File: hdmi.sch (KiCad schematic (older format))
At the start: 0 parts

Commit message: HDMI and VGA circuit added.
Signed-off-by: Kali Prasad <kprasadvnsi@protonmail.com>
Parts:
- added J?: HDMI_A, symbol Connector:HDMI_A
- added R? (x8): 270, symbol Device:R
- added R?: 1K, symbol Device:R
- added R?: R, symbol Device:R
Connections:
- net labels added: +5V, GND
- wire segments 0 -> 33
- no-connect marks 0 -> 4
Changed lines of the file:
@@
 Comment4 ""
 $EndDescr
+$Comp
+L Connector:HDMI_A J?
+U 1 1 5D63985F
+P 8050 3500
+F 0 "J?" H 8480 3546 50  0000 L CNN
+F 1 "HDMI_A" H 8480 3455 50  0000 L CNN
+F 2 "" H 8075 3500 50  0001 C CNN
+F 3 "https://en.wikipedia.org/wiki/HDMI" H 8075 3500 50  0001 C CNN
+	1    8050 3500
+	1    0    0    -1
+$EndComp
+$Comp
+L Device:R R?
+U 1 1 5D63B505
+P 7200 2700
+F 0 "R?" V 7150 2450 50  0000 C CNN
+F 1 "270" V 7150 2900 50  0000 C CNN
+F 2 "" V 7130 2700 50  0001 C CNN
+F 3 "~" H 7200 2700 50  0001 C CNN
+	1    7200 2700
+	0    1    1    0
+$EndComp
+Wire Wire Line
+	7350 2700 7650 2700
+Wire Wire Line
+	7050 2700 6750 2700
+$Comp
+L Device:R R?
+U 1 1 5D63DE7F
+P 7200 2800
+F 0 "R?" V 7150 2550 50  0000 C CNN
+F 1 "270" V 7150 3000 50  0000 C CNN
+F 2 "" V 7130 2800 50  0001 C CNN
+F 3 "~" H 7200 2800 50  0001 C CNN
+	1    7200 2800
+	0    1    1    0
+$EndComp
+Wire Wire Line
+	7350 2800 7650 2800
+Wire Wire Line
+	7050 2800 6750 2800
+$Comp
+L Device:R R?
+U 1 1 5D63FCB8
+P 7200 2900
+F 0 "R?" V 7150 2650 50  0000 C CNN
+F 1 "270" V 7150 3100 50  0000 C CNN
+F 2 "" V 7130 2900 50  0001 C CNN
+F 3 "~" H 7200 2900 50  0001 C CNN
+	1    7200 2900
+	0    1    1    0
+$EndComp
+Wire Wire Line
+	7350 2900 7650 2900
+Wire Wire Line
+	7050 2900 6750 2900
+$Comp
+L Device:R R?
+U 1 1 5D63FCC4
+P 7200 3000
+F 0 "R?" V 7150 2750 50  0000 C CNN
+F 1 "270" V 7150 3200 50  0000 C CNN
+F 2 "" V 7130 3000 50  0001 C CNN
+F 3 "~" H 7200 3000 50  0001 C CNN
+	1    7200 3000
+	0    1    1    0
+$EndComp
+Wire Wire Line
+	7350 3000 7650 3000
+Wire Wire Line
+	7050 3000 6750 3000
+$Comp
+L Device:R R?
+U 1 1 5D6413F6
+P 7200 3100
+F 0 "R?" V 7150 2850 50  0000 C CNN
+F 1 "270" V 7150 3300 50  0000 C CNN
+F 2 "" V 7130 3100 50  0001 C CNN
+F 3 "~" H 7200 3100 50  0001 C CNN
+	1    7200 3100
+	0    1    1    0
+$EndComp
+Wire Wire Line
+	7350 3100 7650 3100
+Wire Wire Line
+	7050 3100 6750 3100
+$Comp
+L Device:R R?
+U 1 1 5D641402
+P 7200 3200
+F 0 "R?" V 7150 2950 50  0000 C CNN
+F 1 "270" V 7150 3400 50  0000 C CNN
+F 2 "" V 7130 3200 50  0001 C CNN
+F 3 "~" H 7200 3200 50  0001 C CNN
+	1    7200 3200
+	0    1    1    0
+$EndComp
+Wire Wire Line
+	7350 3200 7650 3200
+Wire Wire Line
+	7050 3200 6750 3200
+$Comp
+L Device:R R?
+U 1 1 5D64140E
+P 7200 3300
+F 0 "R?" V 7150 3050 50  0000 C CNN
+F 1 "270" V 7150 3500 50  0000 C CNN
+F 2 "" V 7130 3300 50  0001 C CNN
+F 3 "~" H 7200 3300 50  0001 C CNN
+	1    7200 3300
+	0    1    1    0
+$EndComp
+Wire Wire Line
+	7350 3300 7650 3300
+Wire Wire Line
+	7050 3300 6750 3300
+$Comp
+L Device:R R?
+U 1 1 5D64141A
+P 7200 3400
+F 0 "R?" V 7150 3150 50  0000 C CNN
+F 1 "270" V 7150 3600 50  0000 C CNN
+F 2 "" V 7130 3400 50  0001 C CNN
+F 3 "~" H 7200 3400 50  0001 C CNN
+	1    7200 3400
+	0    1    1    0
+$EndComp
+Wire Wire Line
+	7350 3400 7650 3400
+Wire Wire Line
+	7050 3400 6750 3400
+NoConn ~ 7650 3600
+NoConn ~ 7650 3800
+NoConn ~ 7650 3900
+NoConn ~ 7650 4100
+$Comp
+L Device:R R?
+U 1 1 5D64A665
+P 7550 4450
+F 0 "R?" H 7400 4600 50  0000 L CNN
+F 1 "1K" H 7400 4350 50  0000 L CNN
+F 2 "" V 7480 4450 50  0001 C CNN
+F 3 "~" H 7550 4450 50  0001 C CNN
+	1    7550 4450
+	1    0    0    -1
+$EndComp
+Wire Wire Line
+	7650 4200 7550 4200
+Wire Wire Line
+	7550 4200 7550 4300
+$Comp
+L power:GND #PWR?
+U 1 1 5D64BC4F
+P 7550 4700
+F 0 "#PWR?" H 7550 4450 50  0001 C CNN
+F 1 "GND" H 7555 4527 50  0000 C CNN
+F 2 "" H 7550 4700 50  0001 C CNN
+F 3 "" H 7550 4700 50  0001 C CNN
+	1    7550 4700
+	1    0    0    -1
+$EndComp
+Wire Wire Line
+	7550 4600 7550 4700
+Wire Wire Line
+	7850 4600 7850 4700
+Wire Wire Line
+	7850 4700 7950 4700
+Wire Wire Line
+	8350 4700 8350 4600
+Wire Wire Line
+	8250 4600 8250 4700
+Connection ~ 8250 4700
+Wire Wire Line
+	8250 4700 8350 4700
+Wire Wire Line
+	8150 4600 8150 4700
+Connection ~ 8150 4700
+Wire Wire Line
+	8150 4700 8250 4700
+Wire Wire Line
+	8050 4600 8050 4700
+Connection ~ 8050 4700
+Wire Wire Line
+	8050 4700 8150 4700
+Wire Wire Line
+	7950 4600 7950 4700
+Connection ~ 7950 4700
+Wire Wire Line
+	7950 4700 8050 4700
+$Comp
+L power:GND #PWR?
+U 1 1 5D64F8D1
+P 8050 4800
+F 0 "#PWR?" H 8050 4550 50  0001 C CNN
+F 1 "GND" H 8055 4627 50  0000 C CNN
+F 2 "" H 8050 4800 50  0001 C CNN
+F 3 "" H 8050 4800 50  0001 C CNN
+	1    8050 4800
+	1    0    0    -1
+$EndComp
+Wire Wire Line
+	8050 4800 8050 4700
+$Comp
+L Device:R R?
+U 1 1 5D651621
+P 8050 2150
+F 0 "R?" H 8120 2196 50  0000 L CNN
+F 1 "R" H 8120 2105 50  0000 L CNN
+F 2 "" V 7980 2150 50  0001 C CNN
+F 3 "~" H 8050 2150 50  0001 C CNN
+	1    8050 2150
+	1    0    0    -1
+$EndComp
+$Comp
+L power:+5V #PWR?
+U 1 1 5D652459
+P 8050 1900
+F 0 "#PWR?" H 8050 1750 50  0001 C CNN
+F 1 "+5V" H 8065 2073 50  0000 C CNN
+F 2 "" H 8050 1900 50  0001 C CNN
+F 3 "" H 8050 1900 50  0001 C CNN
+	1    8050 1900
+	1    0    0    -1
+$EndComp
+Wire Wire Line
+	8050 2000 8050 1900
+Wire Wire Line
+	8050 2300 8050 2400
 $EndSCHEMATC

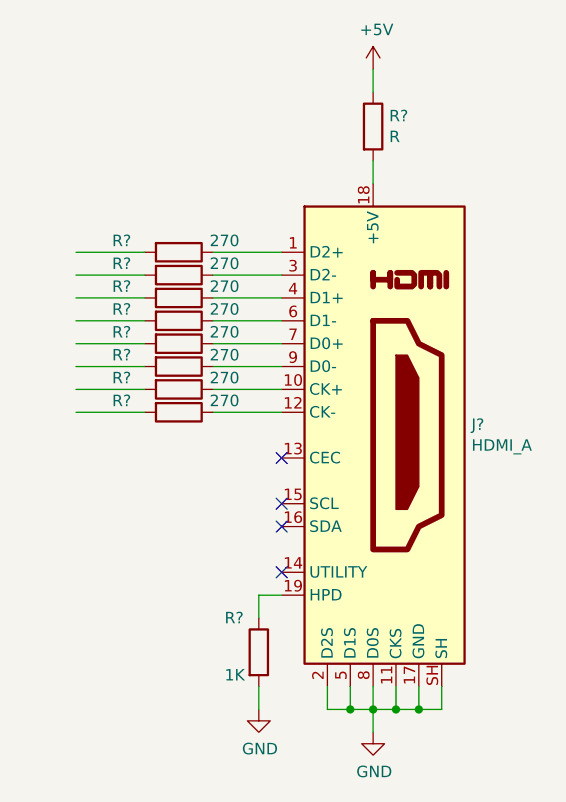
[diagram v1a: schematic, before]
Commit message: SOM added.
Signed-off-by: Kali Prasad <kprasadvnsi@protonmail.com>
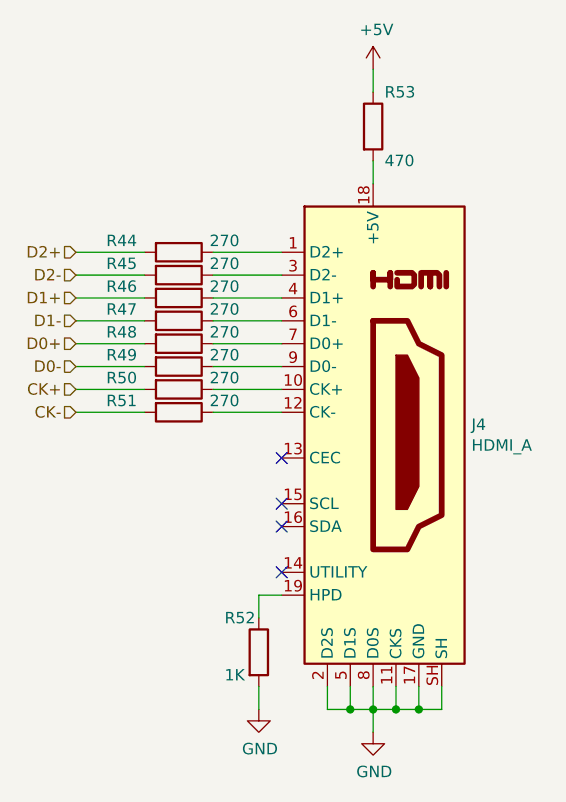
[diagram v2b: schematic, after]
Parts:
- J4: renamed from J?; footprint (none) -> lt_eval_board:HDMI_A_Female_2000-1-2-41-00-BK
- R44, R45, R46, R47, R48, R49, R50, R51, R52: renamed from R?; footprint (none) -> Resistor_SMD:R_0805_2012Metric_Pad1.15x1.40mm_HandSolder
- R53: renamed from R?; value R -> 470; footprint (none) -> Resistor_SMD:R_0805_2012Metric_Pad1.15x1.40mm_HandSolder
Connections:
- net labels added: CK+, CK-, D0+, D0-, D1+, D1-, D2+, D2-
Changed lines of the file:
@@
 $Descr A4 11693 8268
 encoding utf-8
-Sheet 5 7
+Sheet 6 8
 Title "LT_Eval_board"
 Date "2019-06-16"
@@
 $EndDescr
 $Comp
-L Connector:HDMI_A J?
+L Connector:HDMI_A J4
 U 1 1 5D63985F
 P 8050 3500
-F 0 "J?" H 8480 3546 50  0000 L CNN
+F 0 "J4" H 8480 3546 50  0000 L CNN
 F 1 "HDMI_A" H 8480 3455 50  0000 L CNN
-F 2 "" H 8075 3500 50  0001 C CNN
+F 2 "lt_eval_board:HDMI_A_Female_2000-1-2-41-00-BK" H 8075 3500 50  0001 C CNN
 F 3 "https://en.wikipedia.org/wiki/HDMI" H 8075 3500 50  0001 C CNN
 	1    8050 3500
@@
 $EndComp
 $Comp
-L Device:R R?
+L Device:R R44
 U 1 1 5D63B505
 P 7200 2700
-F 0 "R?" V 7150 2450 50  0000 C CNN
+F 0 "R44" V 7150 2450 50  0000 C CNN
 F 1 "270" V 7150 2900 50  0000 C CNN
-F 2 "" V 7130 2700 50  0001 C CNN
+F 2 "Resistor_SMD:R_0805_2012Metric_Pad1.15x1.40mm_HandSolder" V 7130 2700 50  0001 C CNN
 F 3 "~" H 7200 2700 50  0001 C CNN
 	1    7200 2700
@@
 	7050 2700 6750 2700
 $Comp
-L Device:R R?
+L Device:R R45
 U 1 1 5D63DE7F
 P 7200 2800
-F 0 "R?" V 7150 2550 50  0000 C CNN
+F 0 "R45" V 7150 2550 50  0000 C CNN
 F 1 "270" V 7150 3000 50  0000 C CNN
-F 2 "" V 7130 2800 50  0001 C CNN
+F 2 "Resistor_SMD:R_0805_2012Metric_Pad1.15x1.40mm_HandSolder" V 7130 2800 50  0001 C CNN
 F 3 "~" H 7200 2800 50  0001 C CNN
 	1    7200 2800
@@
 	7050 2800 6750 2800
 $Comp
-L Device:R R?
+L Device:R R46
 U 1 1 5D63FCB8
 P 7200 2900
-F 0 "R?" V 7150 2650 50  0000 C CNN
+F 0 "R46" V 7150 2650 50  0000 C CNN
 F 1 "270" V 7150 3100 50  0000 C CNN
-F 2 "" V 7130 2900 50  0001 C CNN
+F 2 "Resistor_SMD:R_0805_2012Metric_Pad1.15x1.40mm_HandSolder" V 7130 2900 50  0001 C CNN
 F 3 "~" H 7200 2900 50  0001 C CNN
 	1    7200 2900
@@
 	7050 2900 6750 2900
 $Comp
-L Device:R R?
+L Device:R R47
 U 1 1 5D63FCC4
 P 7200 3000
-F 0 "R?" V 7150 2750 50  0000 C CNN
+F 0 "R47" V 7150 2750 50  0000 C CNN
 F 1 "270" V 7150 3200 50  0000 C CNN
-F 2 "" V 7130 3000 50  0001 C CNN
+F 2 "Resistor_SMD:R_0805_2012Metric_Pad1.15x1.40mm_HandSolder" V 7130 3000 50  0001 C CNN
 F 3 "~" H 7200 3000 50  0001 C CNN
 	1    7200 3000
@@
 	7050 3000 6750 3000
 $Comp
-L Device:R R?
+L Device:R R48
 U 1 1 5D6413F6
 P 7200 3100
-F 0 "R?" V 7150 2850 50  0000 C CNN
+F 0 "R48" V 7150 2850 50  0000 C CNN
 F 1 "270" V 7150 3300 50  0000 C CNN
-F 2 "" V 7130 3100 50  0001 C CNN
+F 2 "Resistor_SMD:R_0805_2012Metric_Pad1.15x1.40mm_HandSolder" V 7130 3100 50  0001 C CNN
 F 3 "~" H 7200 3100 50  0001 C CNN
 	1    7200 3100
@@
 	7050 3100 6750 3100
 $Comp
-L Device:R R?
+L Device:R R49
 U 1 1 5D641402
 P 7200 3200
-F 0 "R?" V 7150 2950 50  0000 C CNN
+F 0 "R49" V 7150 2950 50  0000 C CNN
 F 1 "270" V 7150 3400 50  0000 C CNN
-F 2 "" V 7130 3200 50  0001 C CNN
+F 2 "Resistor_SMD:R_0805_2012Metric_Pad1.15x1.40mm_HandSolder" V 7130 3200 50  0001 C CNN
 F 3 "~" H 7200 3200 50  0001 C CNN
 	1    7200 3200
@@
 	7050 3200 6750 3200
 $Comp
-L Device:R R?
+L Device:R R50
 U 1 1 5D64140E
 P 7200 3300
-F 0 "R?" V 7150 3050 50  0000 C CNN
+F 0 "R50" V 7150 3050 50  0000 C CNN
 F 1 "270" V 7150 3500 50  0000 C CNN
-F 2 "" V 7130 3300 50  0001 C CNN
+F 2 "Resistor_SMD:R_0805_2012Metric_Pad1.15x1.40mm_HandSolder" V 7130 3300 50  0001 C CNN
 F 3 "~" H 7200 3300 50  0001 C CNN
 	1    7200 3300
@@
 	7050 3300 6750 3300
 $Comp
-L Device:R R?
+L Device:R R51
 U 1 1 5D64141A
 P 7200 3400
-F 0 "R?" V 7150 3150 50  0000 C CNN
+F 0 "R51" V 7150 3150 50  0000 C CNN
 F 1 "270" V 7150 3600 50  0000 C CNN
-F 2 "" V 7130 3400 50  0001 C CNN
+F 2 "Resistor_SMD:R_0805_2012Metric_Pad1.15x1.40mm_HandSolder" V 7130 3400 50  0001 C CNN
 F 3 "~" H 7200 3400 50  0001 C CNN
 	1    7200 3400
@@
 NoConn ~ 7650 4100
 $Comp
-L Device:R R?
+L Device:R R52
 U 1 1 5D64A665
 P 7550 4450
-F 0 "R?" H 7400 4600 50  0000 L CNN
+F 0 "R52" H 7400 4600 50  0000 L CNN
 F 1 "1K" H 7400 4350 50  0000 L CNN
-F 2 "" V 7480 4450 50  0001 C CNN
+F 2 "Resistor_SMD:R_0805_2012Metric_Pad1.15x1.40mm_HandSolder" V 7480 4450 50  0001 C CNN
 F 3 "~" H 7550 4450 50  0001 C CNN
 	1    7550 4450
@@
 	7550 4200 7550 4300
 $Comp
-L power:GND #PWR?
+L power:GND #PWR016
 U 1 1 5D64BC4F
 P 7550 4700
-F 0 "#PWR?" H 7550 4450 50  0001 C CNN
+F 0 "#PWR016" H 7550 4450 50  0001 C CNN
 F 1 "GND" H 7555 4527 50  0000 C CNN
 F 2 "" H 7550 4700 50  0001 C CNN
@@
 	7950 4700 8050 4700
 $Comp
-L power:GND #PWR?
+L power:GND #PWR018
 U 1 1 5D64F8D1
 P 8050 4800
-F 0 "#PWR?" H 8050 4550 50  0001 C CNN
+F 0 "#PWR018" H 8050 4550 50  0001 C CNN
 F 1 "GND" H 8055 4627 50  0000 C CNN
 F 2 "" H 8050 4800 50  0001 C CNN
@@
 	8050 4800 8050 4700
 $Comp
-L Device:R R?
+L Device:R R53
 U 1 1 5D651621
 P 8050 2150
-F 0 "R?" H 8120 2196 50  0000 L CNN
-F 1 "R" H 8120 2105 50  0000 L CNN
-F 2 "" V 7980 2150 50  0001 C CNN
+F 0 "R53" H 8100 2300 50  0000 L CNN
+F 1 "470" H 8100 2000 50  0000 L CNN
+F 2 "Resistor_SMD:R_0805_2012Metric_Pad1.15x1.40mm_HandSolder" V 7980 2150 50  0001 C CNN
 F 3 "~" H 8050 2150 50  0001 C CNN
 	1    8050 2150
@@
 $EndComp
 $Comp
-L power:+5V #PWR?
+L power:+5V #PWR017
 U 1 1 5D652459
 P 8050 1900
-F 0 "#PWR?" H 8050 1750 50  0001 C CNN
+F 0 "#PWR017" H 8050 1750 50  0001 C CNN
 F 1 "+5V" H 8065 2073 50  0000 C CNN
 F 2 "" H 8050 1900 50  0001 C CNN
@@
 Wire Wire Line
 	8050 2300 8050 2400
+Text HLabel 6750 2700 0    50   Input ~ 0
+D2+
+Text HLabel 6750 2800 0    50   Input ~ 0
+D2-
+Text HLabel 6750 2900 0    50   Input ~ 0
+D1+
+Text HLabel 6750 3000 0    50   Input ~ 0
+D1-
+Text HLabel 6750 3100 0    50   Input ~ 0
+D0+
+Text HLabel 6750 3200 0    50   Input ~ 0
+D0-
+Text HLabel 6750 3300 0    50   Input ~ 0
+CK+
+Text HLabel 6750 3400 0    50   Input ~ 0
+CK-
 $EndSCHEMATC
